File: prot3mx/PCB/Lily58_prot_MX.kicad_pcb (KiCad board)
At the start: 2 copper layers, 142.5 x 106.3 mm, 115 parts, among them J1 LED, J2 4PIN, J3 OLED, P1 i2c_pin, P2 i2c_pin, SW1 SW_PUSH, SW10 SW_PUSH, SW11 SW_PUSH, SW12 SW_PUSH, SW13 SW_PUSH, SW14 SW_PUSH, SW15 SW_PUSH, SW16 SW_PUSH, SW17 SW_PUSH, SW18 SW_PUSH, SW19 SW_PUSH, SW2 SW_PUSH, SW20 SW_PUSH, SW21 SW_PUSH, SW22 SW_PUSH, SW23 SW_PUSH, SW24 SW_PUSH, SW25 SW_PUSH, SW26 SW_PUSH, SW27 SW_PUSH, SW28 SW_PUSH, SW29 SW_PUSH, SW3 SW_PUSH, SW30 ROT_ENC_SW, SW31 ROT_ENC_SW, SW32 ROT_ENC_SW, SW4 SW_PUSH, SW5 SW_PUSH, SW6 SW_PUSH, SW7 SW_PUSH, SW8 SW_PUSH, SW9 SW_PUSH, U1 ProMicro

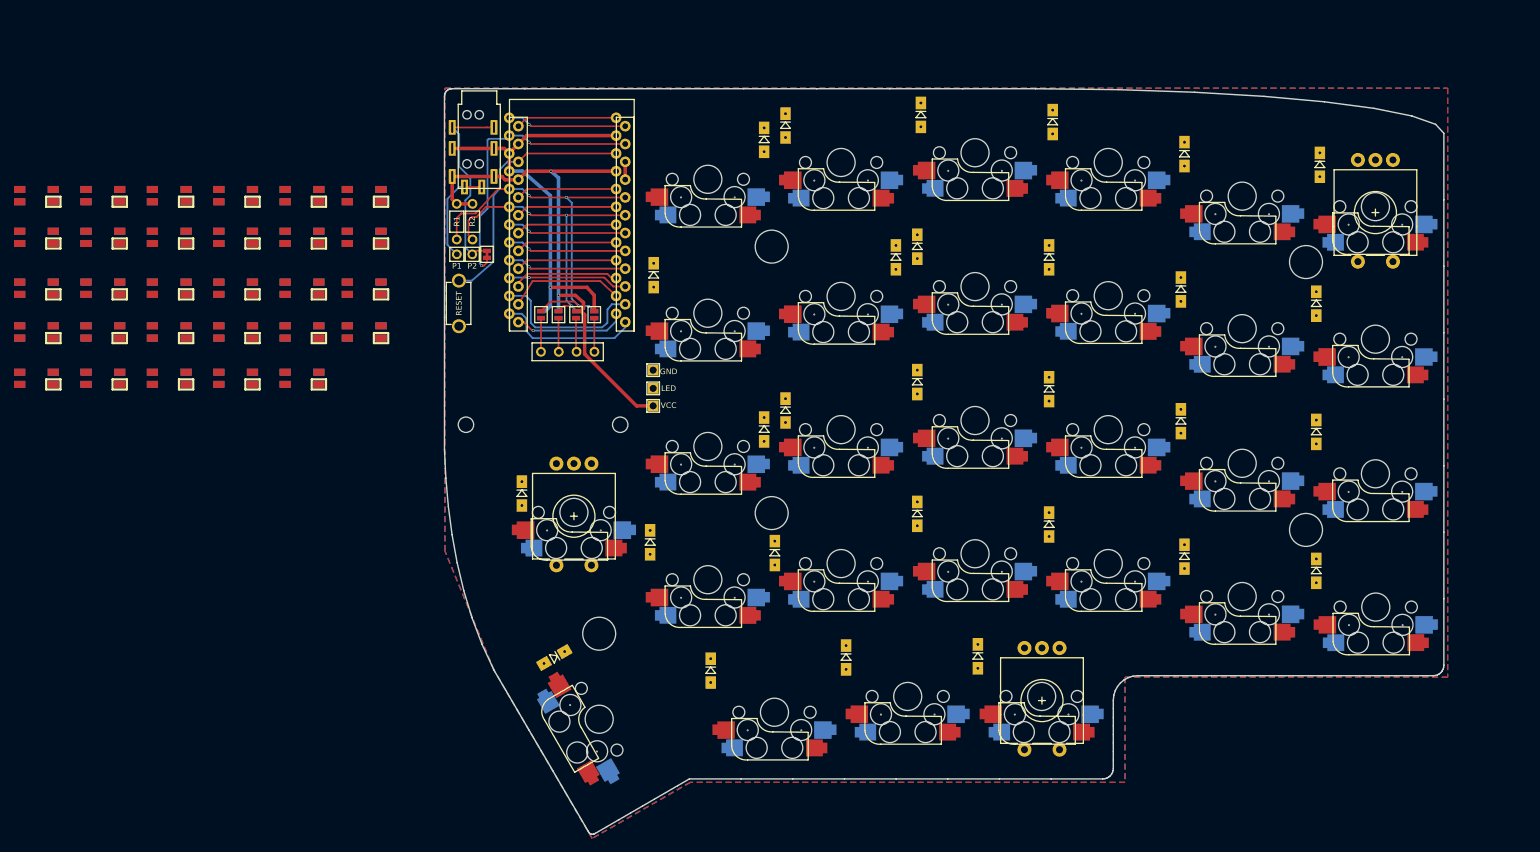
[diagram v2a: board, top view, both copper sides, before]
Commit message: repositioned diodes, using original LED footprints
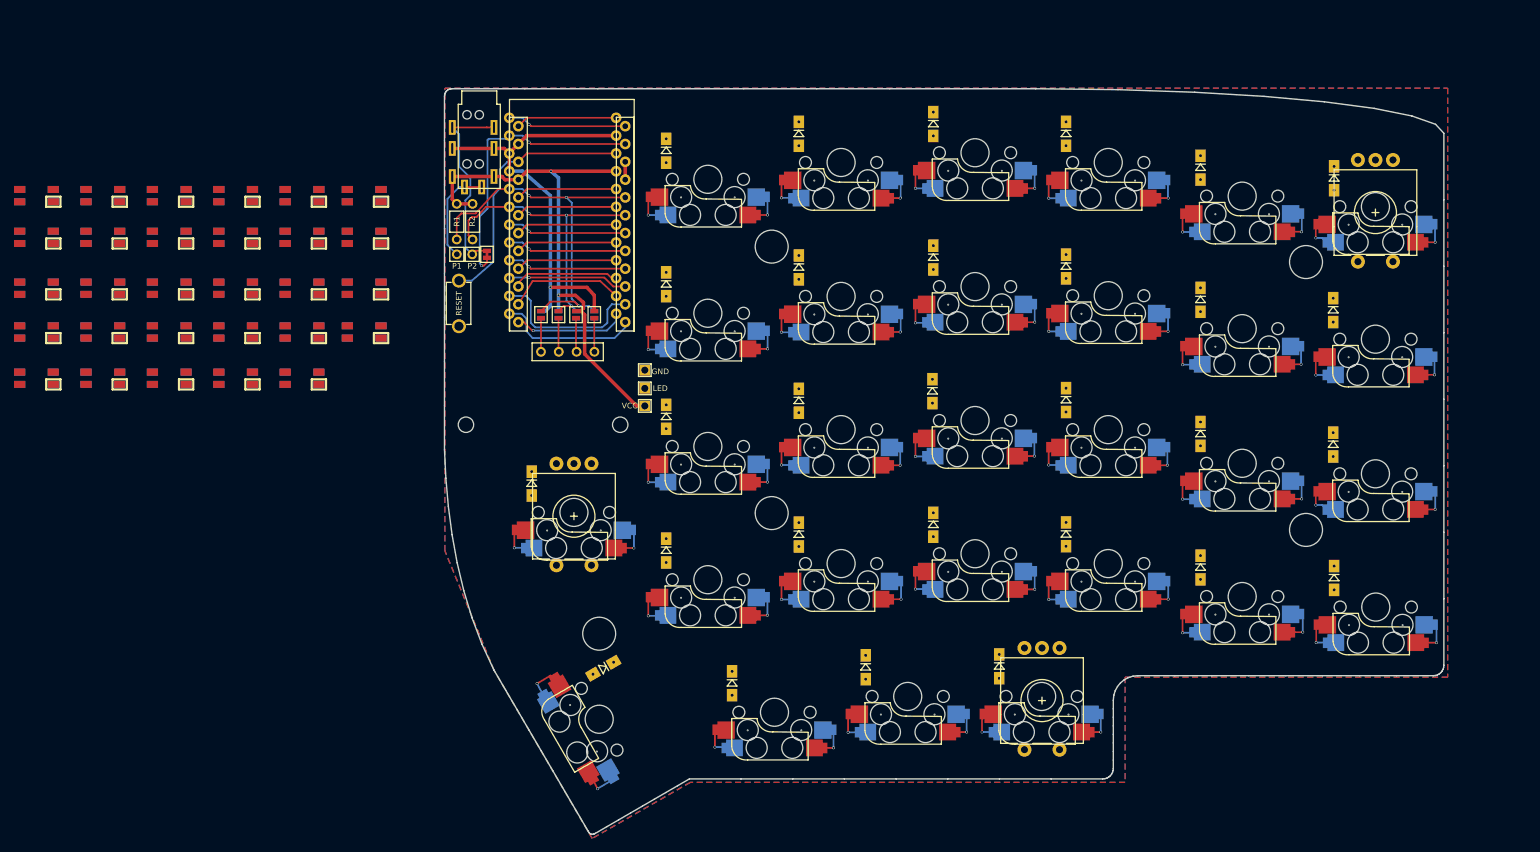
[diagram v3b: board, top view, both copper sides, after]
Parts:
- L1, L10, L11, L12, L13, L14, L15, L16, L17, L18, L19, L2, L20, L21, L22, L23, L24, L25, L26, L27, L28, L29, L3, L4, L5, L6, L7, L8, L9: footprint Lily58_prot_MX-footprint:SK6812MINI_rev_w_co -> Lily58_prot_MX-footprint:SK6812MINI_rev
- moved D13 14.1 mm to (114.6, 83.9)
- moved D1 14.1 mm to (114.6, 45.9)
- moved D8 13.9 mm to (133.5, 62.6)
- moved D26 7.15 mm to (105.6, 119.7)
- moved D20 4.33 mm to (133.5, 100.7)
- moved D27 3.54 mm to (124.0, 121.9)
- moved D29 3.37 mm to (162.1, 119.5)
- moved D17 3.33 mm to (190.8, 86.3)
- moved D11 3.16 mm to (190.8, 67.2)
- moved D28 3.12 mm to (143.0, 119.6)
- moved D18 3.01 mm to (209.7, 87.8)
- moved D5 2.99 mm to (190.8, 48.3)
- moved D16 2.87 mm to (171.6, 81.5)
- moved D6 2.81 mm to (209.8, 49.9)
- moved D22 2.79 mm to (171.6, 100.6)
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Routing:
- net col4: track 16.6 -> 51.8 mm, vias 0 -> 5
- net col2: track 14.4 -> 49.5 mm, vias 0 -> 5
- net R1_SW2: track 16.1 -> 51.1 mm, vias 1 -> 6
- net R2_SW2: track 14.4 -> 49.5 mm, vias 0 -> 5
- net col3: track 15.3 -> 50.2 mm, vias 0 -> 5
- net R3_SW2: track 14.4 -> 42.7 mm, vias 0 -> 4
- net Net-(D26-Pad2): track 0.00 -> 7.63 mm, vias 0 -> 1
- net Net-(D7-Pad2): track 0.00 -> 7.14 mm, vias 0 -> 1
- net Net-(D9-Pad2): track 0.00 -> 7.13 mm, vias 0 -> 1
- net Net-(D23-Pad2): track 0.00 -> 7.12 mm, vias 0 -> 1
- net Net-(D19-Pad2): track 0.00 -> 7.10 mm, vias 0 -> 1
- net Net-(D11-Pad2): track 0.00 -> 7.08 mm, vias 0 -> 1
- net Net-(D15-Pad2): track 0.00 -> 7.05 mm, vias 0 -> 1
- net Net-(D20-Pad2): track 0.00 -> 7.05 mm, vias 0 -> 1
- net Net-(D22-Pad2): track 0.00 -> 7.05 mm, vias 0 -> 1
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
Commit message: replaced hotswap footprint with TH footprint where encoder footprint overlaps
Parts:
- SW25, SW29, SW6: footprint Lily58_prot_MX-footprint:MX_Hotswap -> Lily58_prot_MX-footprint:MX_FLIP_HOLES
- moved L6 144.2 mm to (215.7, 49.7)
- moved SW32 0.84 mm to (215.7, 53.9)
- moved SW31 0.59 mm to (168.1, 123.8)
- moved SW30 0.54 mm to (101.4, 97.5)
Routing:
- net col4: track 51.8 -> 75.9 mm, vias 5 -> 6
- net col3: track 50.2 -> 73.0 mm, vias 5 -> 6
- net col2: track 49.5 -> 69.6 mm, vias 5 -> 6
- net row0: track 17.0 -> 36.8 mm
- net row2: track 17.1 -> 36.4 mm
- net R1_SW2: track 51.1 -> 33.0 mm, vias 6 -> 4
- net R2_SW2: track 49.5 -> 64.3 mm
- net row3: track 22.7 -> 35.8 mm
- net R3_SW2: track 42.7 -> 54.0 mm
- net GND: track 63.4 -> 72.4 mm
- net R3_SW1: track 5.65 -> 12.9 mm, vias 1 -> 0
- net R2_SW1: track 6.99 -> 13.2 mm, vias 1 -> 0
- net row1: track 17.0 -> 23.1 mm
- net R1_SW1: track 6.98 -> 12.9 mm, vias 1 -> 0
- net VCC: track 75.6 -> 81.2 mm
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
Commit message: removed per-key-LEG in favour of underglow only
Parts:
- removed L11, L12, L13, L14, L15, L16, L17, L18, L19, L20, L21, L22, L23, L24, L25, L26, L27, L28, L29: SK6812MINI, Lily58_prot_MX-footprint:SK6812MINI_rev
- removed the L5 at (62.6, 52.3)
- removed the L8 at (34.2, 58.3)
- L1, L2, L3, L4, L6: footprint Lily58_prot_MX-footprint:SK6812MINI_rev -> Lily58_prot_MX-footprint:SK6812MINI_underglow_rev
- L5: renamed from L7; footprint Lily58_prot_MX-footprint:SK6812MINI_rev -> Lily58_prot_MX-footprint:SK6812MINI_underglow_rev
- L7: renamed from L9; footprint Lily58_prot_MX-footprint:SK6812MINI_rev -> Lily58_prot_MX-footprint:SK6812MINI_underglow_rev
- L8: renamed from L10; footprint Lily58_prot_MX-footprint:SK6812MINI_rev -> Lily58_prot_MX-footprint:SK6812MINI_underglow_rev
- SW25, SW29, SW6: footprint Lily58_prot_MX-footprint:MX_FLIP_HOLES -> Lily58_prot_MX-footprint:MX_Hotswap
- moved L5 189.3 mm to (212.4, 82.6)
- moved L4 150.8 mm to (203.9, 48.5)
- moved L3 122.2 mm to (165.5, 43.0)
- moved L7 110.7 mm to (135.6, 120.0)
- moved L2 91.7 mm to (125.7, 45.1)
- moved L1 75.6 mm to (94.9, 80.5)
- moved L6 74.8 mm to (177.7, 114.0)
- moved L8 74.0 mm to (106.7, 109.4)
- moved SW30 0.50 mm to (101.4, 98.0)
- moved SW31 0.50 mm to (168.1, 124.2)
- moved SW32 0.50 mm to (215.7, 54.4)
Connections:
- L5 pad 1: Net-(L7-Pad1) (its old number) -> Net-(L5-Pad1)
- L5 pad 3: Net-(L6-Pad1) -> Net-(L4-Pad1)
- L7 pad 3: Net-(L8-Pad1) (its old number) -> Net-(L6-Pad1)
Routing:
- net R1_SW2: track 33.0 -> 81.7 mm, vias 4 -> 6
- net row4: track 23.8 -> 46.3 mm
- net row3: track 35.8 -> 54.5 mm, vias 0 -> 1
- net R2_SW2: track 64.3 -> 73.1 mm, vias 5 -> 6
- net R3_SW2: track 54.0 -> 61.1 mm, vias 4 -> 5
- net R2_SW1: track 13.2 -> 17.2 mm, vias 0 -> 1
- net R3_SW1: track 12.9 -> 16.6 mm, vias 0 -> 1
- net R1_SW1: track 12.9 -> 16.3 mm, vias 0 -> 1
- net col4: track 75.9 -> 74.2 mm
- net row0: track 36.8 -> 35.4 mm
- net SDA: track 54.3 -> 53.4 mm
- net col3: track 73.0 -> 73.9 mm
- net GND: track 72.4 -> 71.6 mm
- net col2: track 69.6 -> 68.9 mm
- net row2: track 36.4 -> 36.9 mm

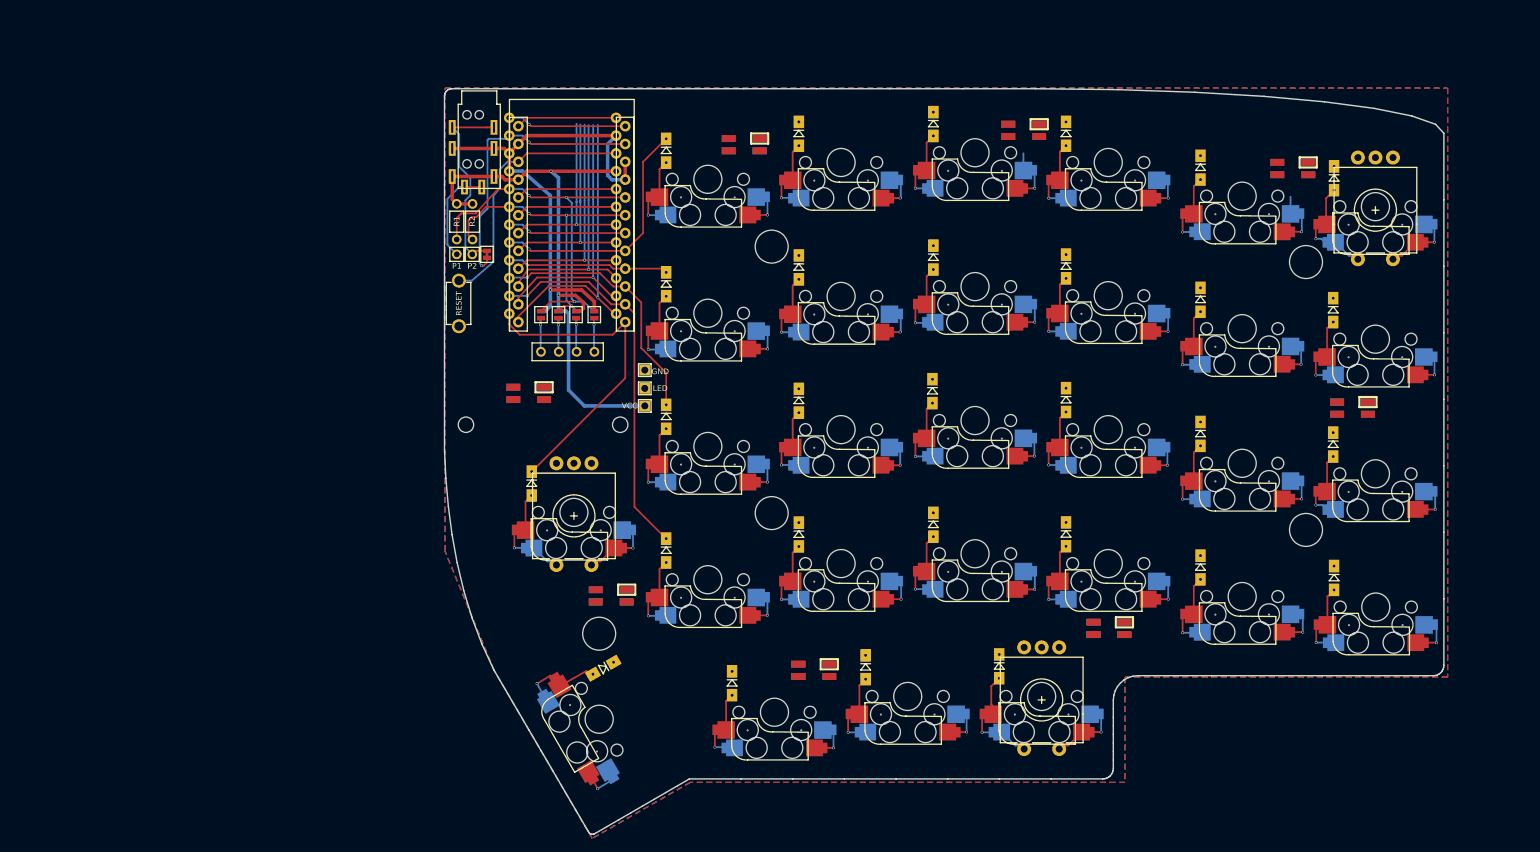
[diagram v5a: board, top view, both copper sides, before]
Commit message: routing nearly complete; some ground pads need connecting
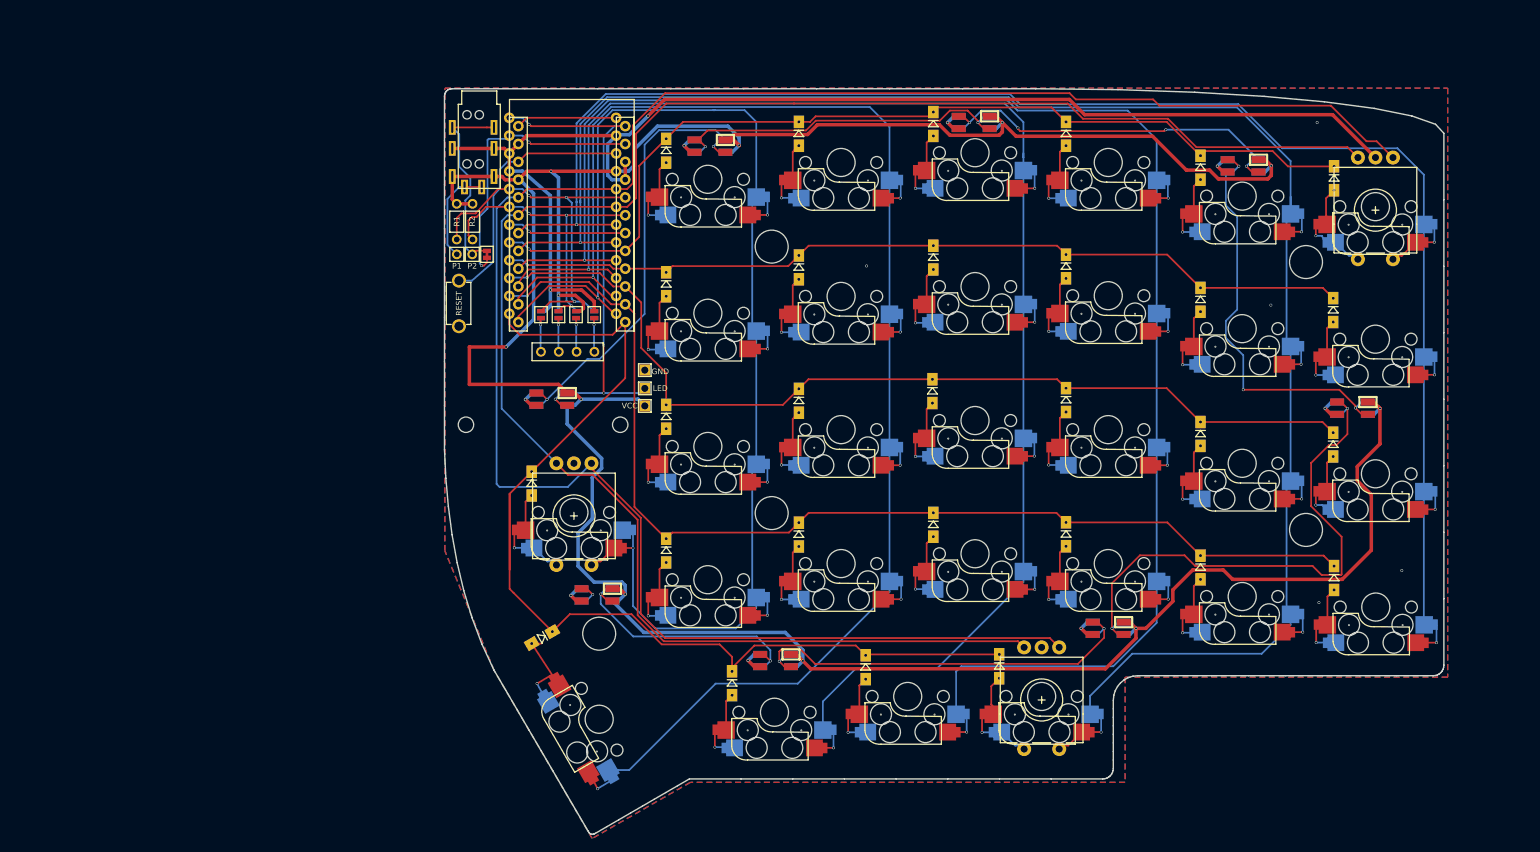
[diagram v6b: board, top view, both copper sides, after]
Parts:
- moved D26 9.77 mm to (96.8, 115.4)
- moved L3 7.16 mm to (158.5, 41.9)
- moved L4 7.09 mm to (196.8, 48.1)
- moved L7 5.63 mm to (130.2, 118.6)
- moved L2 4.88 mm to (120.8, 45.3)
- moved L1 3.39 mm to (98.2, 81.4)
- moved L8 2.04 mm to (104.7, 109.3)
- moved L6 0.11 mm to (177.6, 114.0)
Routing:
- net VCC: track 81.2 -> 443.3 mm, vias 2 -> 11
- net R_A: track 14.4 -> 283.7 mm
- net R_B: track 14.4 -> 261.0 mm
- net R2_SW2: track 73.1 -> 282.3 mm
- net col2: track 68.9 -> 260.7 mm
- net R3_SW2: track 61.1 -> 252.7 mm
- net col3: track 73.9 -> 241.8 mm
- net col4: track 74.2 -> 237.1 mm
- net GND: track 71.6 -> 216.6 mm, vias 1 -> 15
- net R1_SW2: track 81.7 -> 204.8 mm
- net row4: track 46.3 -> 155.5 mm
- net row0: track 35.4 -> 136.6 mm
- net row3: track 54.5 -> 154.5 mm
- net row1: track 23.1 -> 122.9 mm
- net row2: track 36.9 -> 136.7 mm
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
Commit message: grouped diodes and re-routed all switch traces; considering removing underglow in favour of single top-mounted layer indicating LED
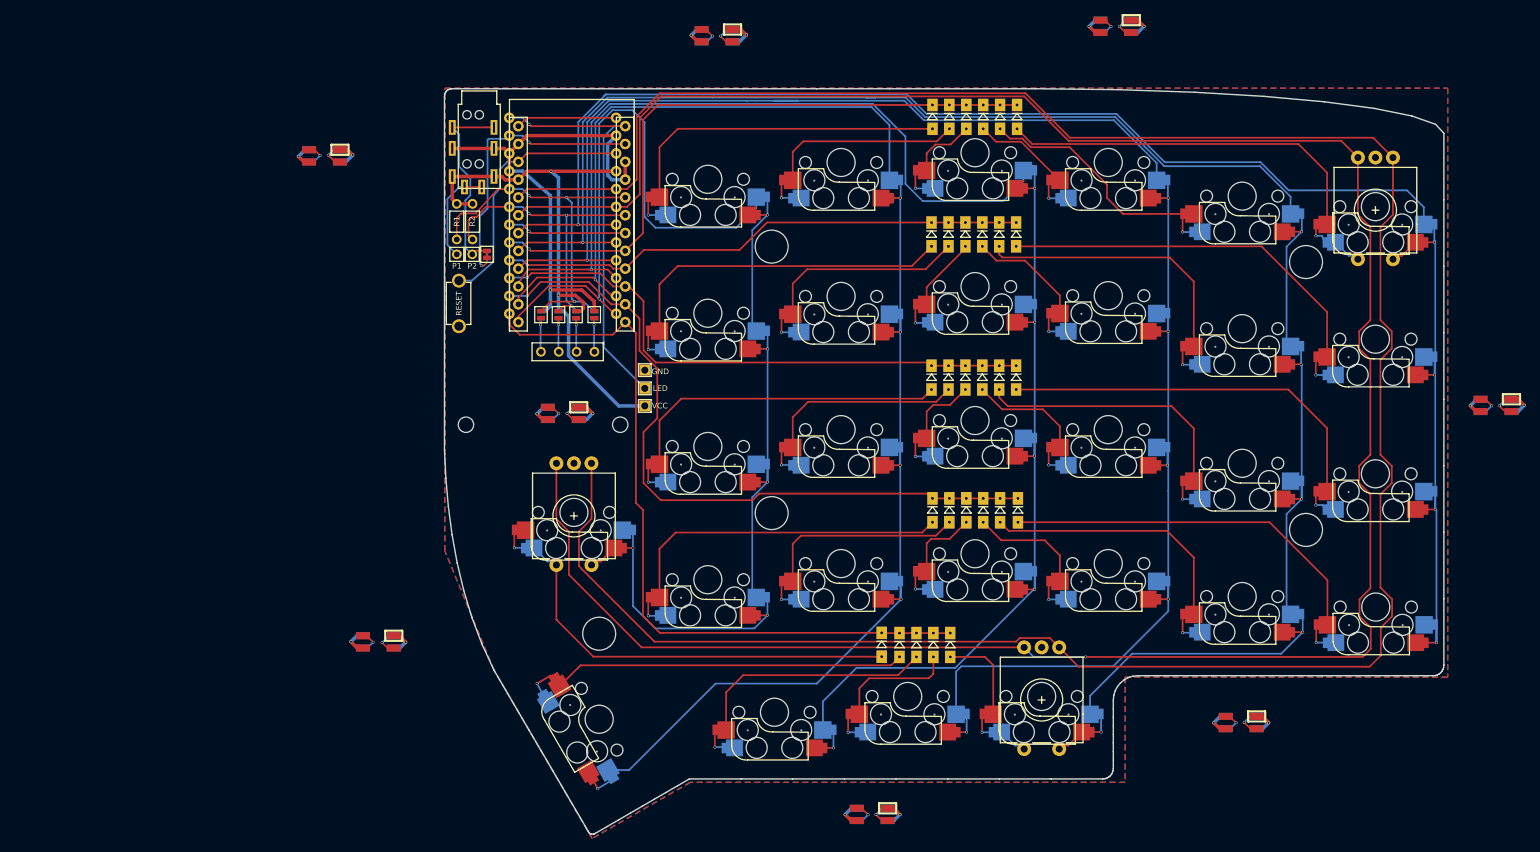
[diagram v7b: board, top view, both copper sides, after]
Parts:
- moved L8 73.7 mm to (65.8, 46.7)
- moved L7 56.7 mm to (73.5, 116.0)
- moved D25 55.0 mm to (145.3, 116.4)
- moved D26 51.0 mm to (147.8, 116.4), turned to 270 degrees
- moved L4 49.7 mm to (232.9, 82.2)
- moved L5 47.6 mm to (196.6, 127.5)
- moved D12 46.5 mm to (164.5, 57.9)
- moved D18 46.2 mm to (164.5, 78.3)
- moved D24 46.1 mm to (164.7, 97.2)
- moved D6 46.1 mm to (164.6, 41.1)
- moved L6 42.9 mm to (143.9, 140.6)
- moved D7 38.5 mm to (152.4, 57.9)
- moved D19 38.4 mm to (152.5, 97.2)
- moved D1 38.3 mm to (152.5, 41.1)
- moved D13 38.3 mm to (152.4, 78.3)
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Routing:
- net VCC: track 443.3 -> 113.4 mm, vias 11 -> 10
- net GND: track 216.6 -> 102.8 mm, vias 15 -> 9
- net R_B: track 261.0 -> 347.9 mm, vias 0 -> 1
- net Net-(L5-Pad1): track 78.0 -> 7.75 mm
- net R_A: track 283.7 -> 352.5 mm
- net Net-(L1-Pad1): track 64.0 -> 7.99 mm
- net row2: track 136.7 -> 82.2 mm
- net row3: track 154.5 -> 102.0 mm
- net Net-(L6-Pad1): track 59.7 -> 8.03 mm
- net R1_SW1: track 16.3 -> 67.4 mm
- net Net-(L4-Pad1): track 59.0 -> 8.18 mm, vias 3 -> 2
- net Net-(D18-Pad2): track 12.2 -> 62.5 mm
- net Net-(D12-Pad2): track 12.4 -> 61.7 mm
- net Net-(D24-Pad2): track 12.4 -> 60.9 mm
- net row4: track 155.5 -> 107.2 mm
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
